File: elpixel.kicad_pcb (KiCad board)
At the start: 2 copper layers, 20 x 14 mm, 5 parts

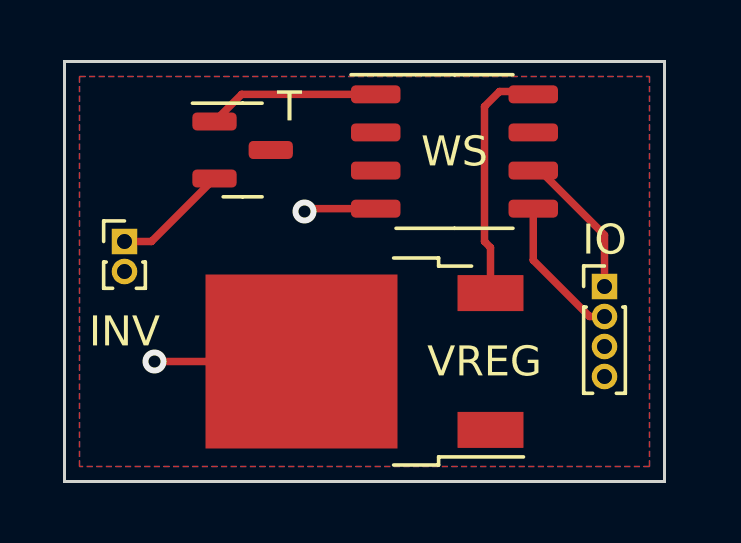
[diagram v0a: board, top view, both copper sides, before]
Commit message: new version with different input/output pins to make the external wiring easier
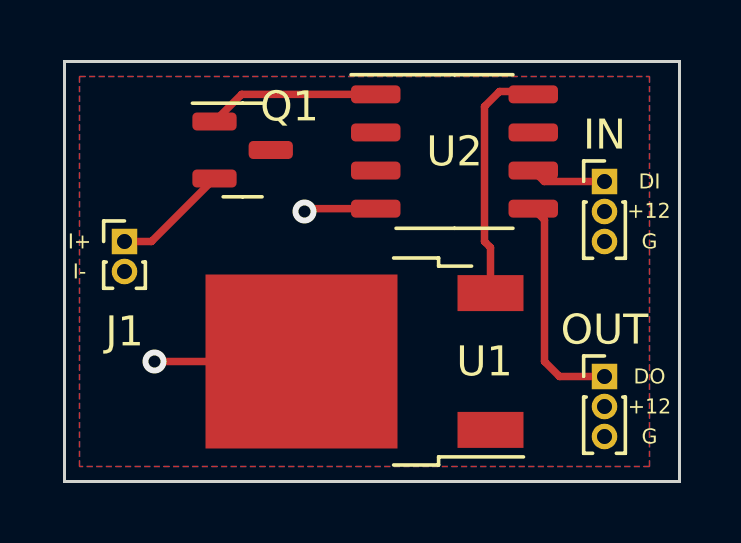
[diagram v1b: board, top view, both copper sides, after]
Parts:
- removed IO: Conn_01x04, Connector_PinHeader_1.00mm:PinHeader_1x04_P1.00mm_Vertical
- added IN: Conn_01x03, Connector_PinHeader_1.00mm:PinHeader_1x03_P1.00mm_Vertical, F.Cu at (125.0, 133.0)
- added OUT: Conn_01x03, Connector_PinHeader_1.00mm:PinHeader_1x03_P1.00mm_Vertical, F.Cu at (125.0, 139.5)
- renumbered INV to J1, T to Q1, VREG to U1, WS to U2
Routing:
- net Net-(U2-Pad5): track 4.87 -> 7.46 mm
- net Net-(U2-Pad6): track 4.98 -> 2.75 mm
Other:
- board size 20 x 14 mm -> 20.5 x 14 mm
- board text added: "+12"
- board text added: "DI"
- board text added: "DO"
- board text added: "G"
- board text added: "I+"
- board text added: "I-"

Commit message: updated schematic for 6v passthrough
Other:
- board text added: "INV+"
- board text added: "INV-"
- board text removed: "I+"
- board text removed: "I-"
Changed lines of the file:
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@@
     (effects (font (size 0.5 0.5) (thickness 0.1)) (justify mirror))
   )
-  (gr_text "I+\n" (at 107.480179 134.979988) (layer "B.SilkS")
+  (gr_text "INV+\n" (at 110.5 135) (layer "B.SilkS")
     (effects (font (size 0.5 0.5) (thickness 0.1)) (justify mirror))
   )
-  (gr_text "I-" (at 107.480179 135.979988) (layer "B.SilkS")
+  (gr_text "INV-" (at 110.5 136) (layer "B.SilkS")
     (effects (font (size 0.5 0.5) (thickness 0.1)) (justify mirror))
   )
@@
     (effects (font (size 0.5 0.5) (thickness 0.1)) (justify mirror))
   )
-  (gr_text "I-" (at 107.5 136) (layer "F.SilkS")
+  (gr_text "INV-" (at 111 136) (layer "F.SilkS")
     (effects (font (size 0.5 0.5) (thickness 0.1)))
   )
@@
     (effects (font (size 0.5 0.5) (thickness 0.1)))
   )
-  (gr_text "I+\n" (at 107.5 135) (layer "F.SilkS")
+  (gr_text "INV+" (at 111 135) (layer "F.SilkS")
     (effects (font (size 0.5 0.5) (thickness 0.1)))
   )

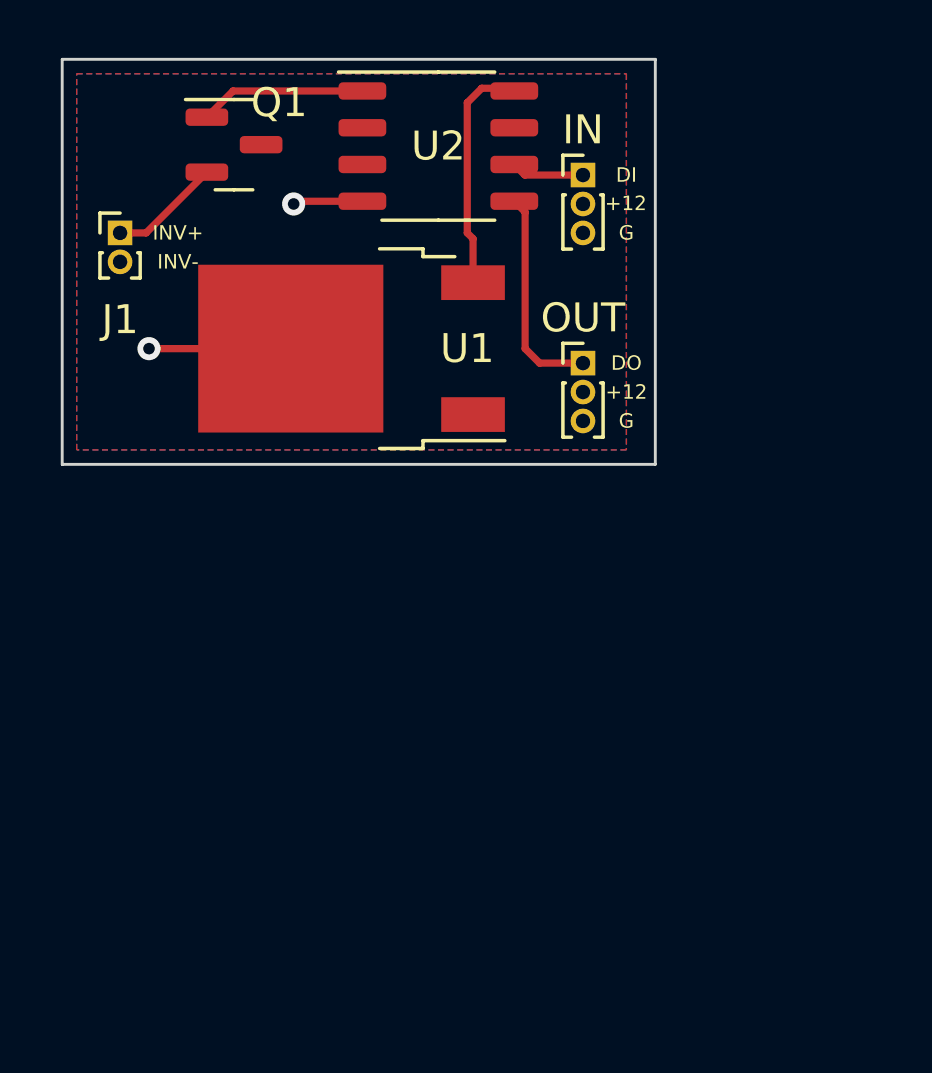
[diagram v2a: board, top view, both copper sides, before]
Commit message: prototype new 4 wire version without mosfet.
I should probably add the mosfet back though in case I decide I do want
a 12v only system?
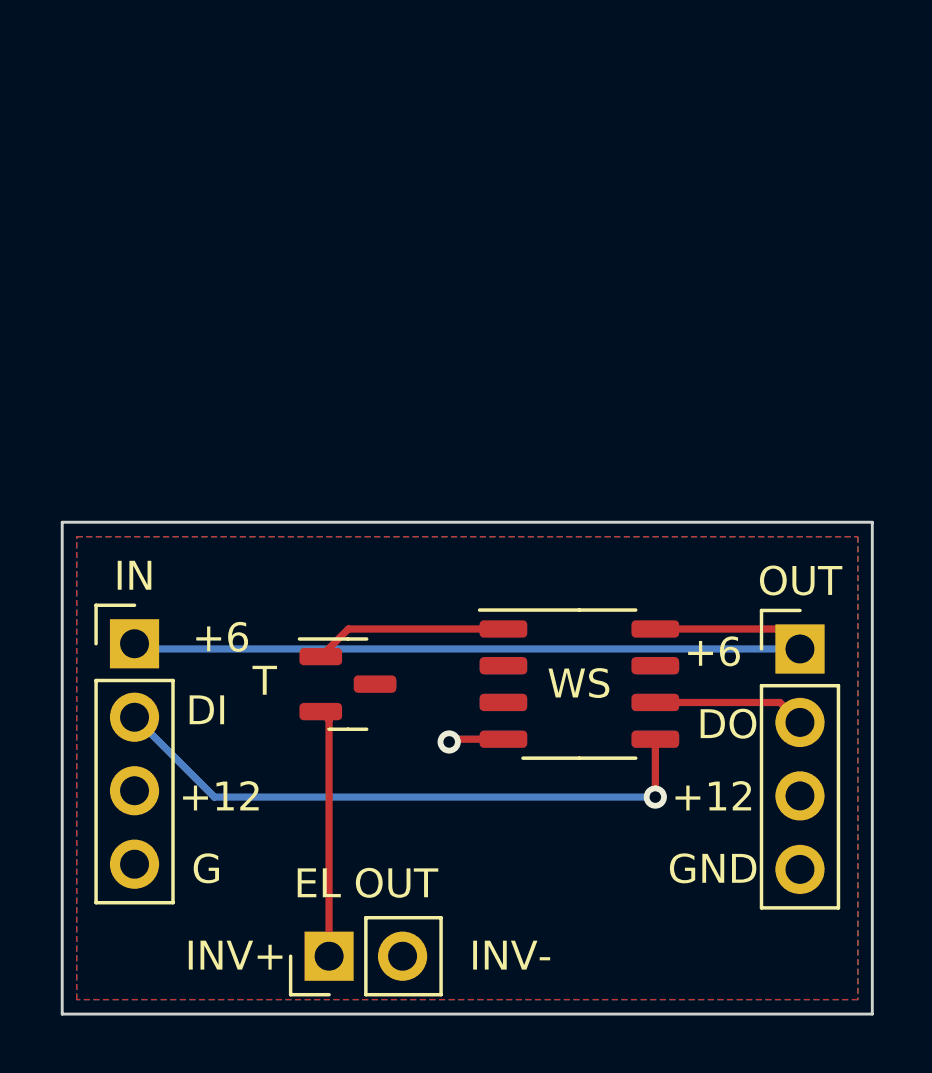
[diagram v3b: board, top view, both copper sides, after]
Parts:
- removed the IN at (125.0, 133.0)
- removed the OUT at (125.0, 139.5)
- removed U1: MC78M05_TO252, Package_TO_SOT_SMD:TO-252-2
- added IN: Conn_01x04, Connector_PinHeader_2.54mm:PinHeader_1x04_P2.54mm_Vertical, F.Cu at (109.5, 149.2)
- added OUT: Conn_01x04, Connector_PinHeader_2.54mm:PinHeader_1x04_P2.54mm_Vertical, F.Cu at (132.5, 149.4)
- EL OUT: renamed from J1; footprint Connector_PinHeader_1.00mm:PinHeader_1x02_P1.00mm_Vertical -> Connector_PinHeader_2.54mm:PinHeader_1x02_P2.54mm_Vertical
- moved EL OUT 26.0 mm to (116.2, 160.0), turned to 90 degrees
- moved WS 19.2 mm to (124.9, 150.6)
- moved T 19.1 mm to (116.9, 150.6)
- renumbered Q1 to T, U2 to WS
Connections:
- WS pad 8: Net-(U1-Pad3) -> +6V
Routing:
- net +6V: track 0.00 -> 28.4 mm
- net Net-(U2-Pad5): track 7.46 -> 21.1 mm, vias 0 -> 1
- net Net-(U1-Pad3): track 8.04 -> 0.00 mm
- net GND: track 7.31 -> 1.91 mm, vias 2 -> 1
- net Net-(J1-Pad1): track 3.87 -> 8.57 mm
- net Net-(U2-Pad6): track 2.75 -> 5.29 mm
- net Net-(U2-Pad1): track 5.75 -> 6.71 mm
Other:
- board size 20.5 x 14 mm -> 28 x 17 mm
- board text added: "+6"
- board text added: "GND"
